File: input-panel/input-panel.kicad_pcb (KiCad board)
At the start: 2 copper layers, 81.3 x 54.6 mm, 11 parts, among them J1 Conn_01x07_Male

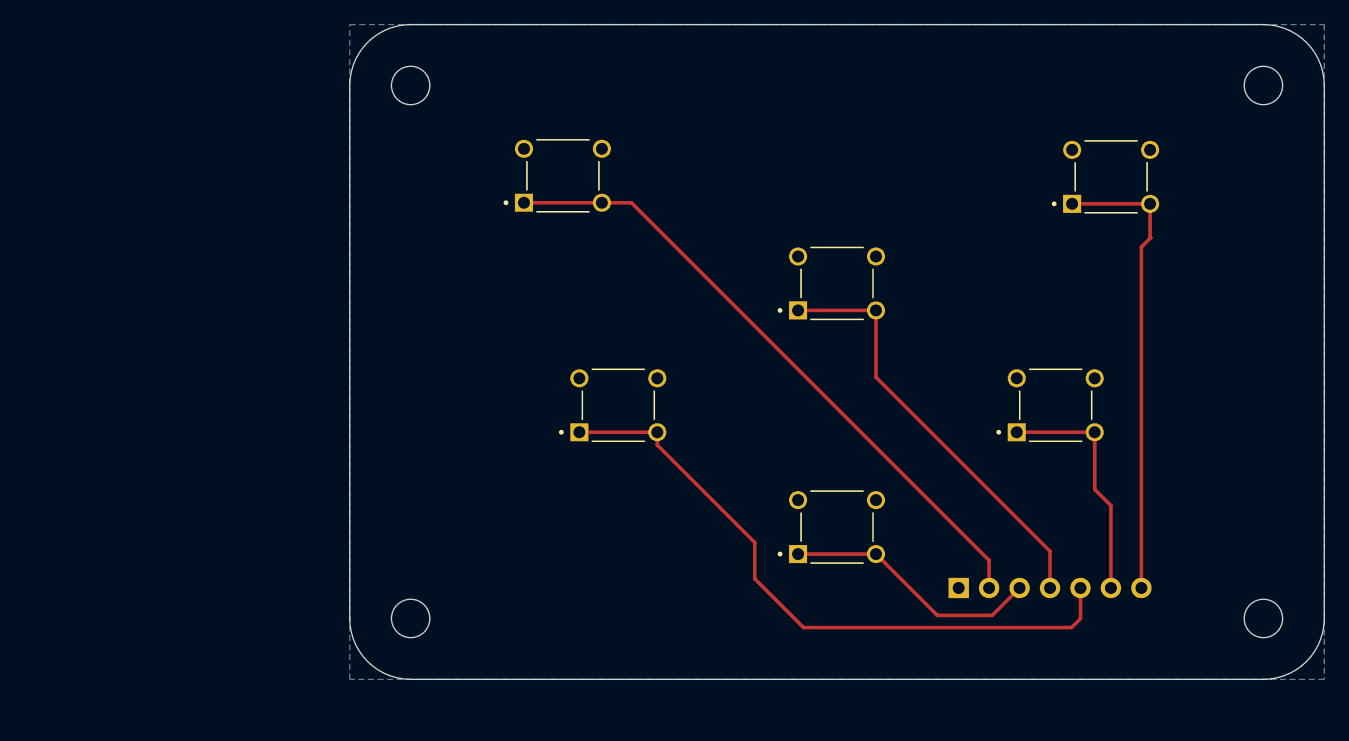
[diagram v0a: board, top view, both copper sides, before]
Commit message: re-designed input panel PCB
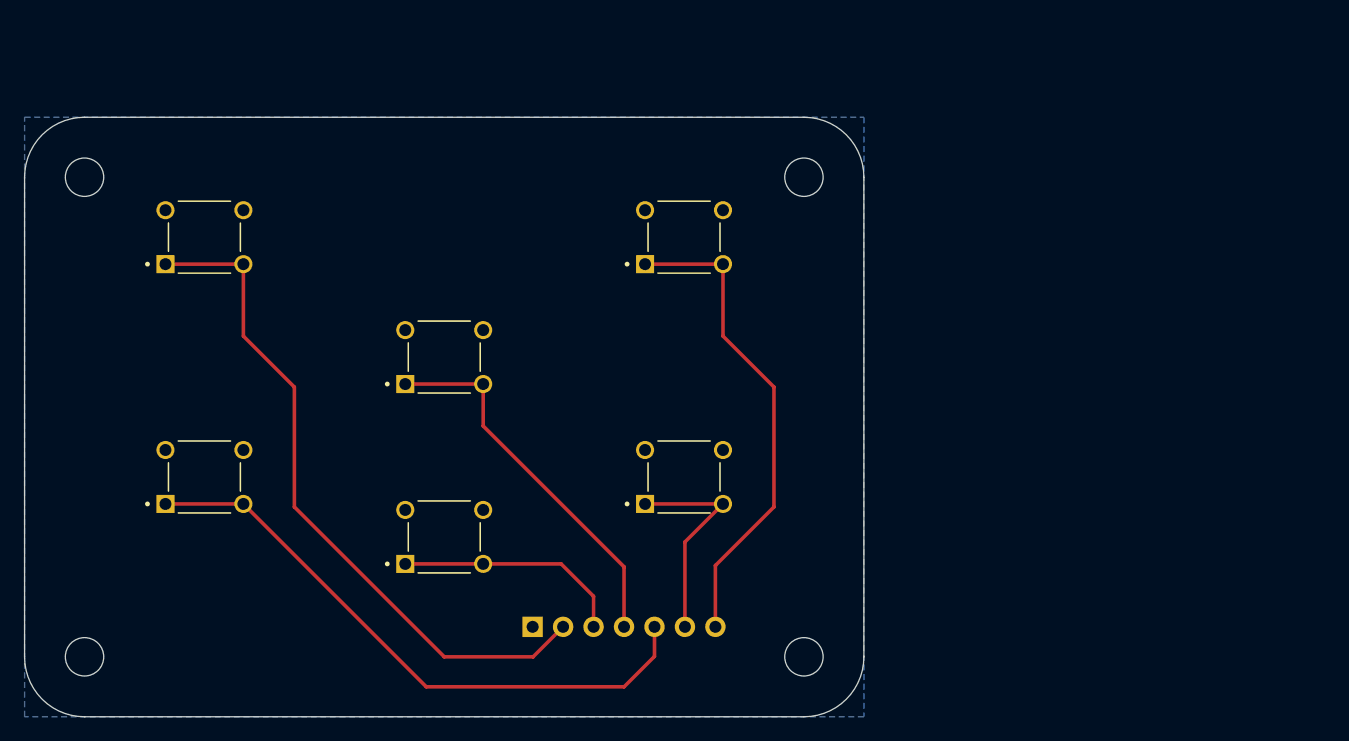
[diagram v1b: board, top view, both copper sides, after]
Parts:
- moved H4 39.1 mm to (172.5, 77.5)
- moved H2 38.5 mm to (172.5, 117.5)
- moved S6 36.0 mm to (162.5, 82.5)
- moved J1 35.7 mm to (149.9, 115.0)
- moved S4 35.0 mm to (122.5, 102.5)
- moved S3 33.3 mm to (142.5, 92.5)
- moved S2 32.8 mm to (142.5, 107.5)
- moved S5 31.6 mm to (162.5, 102.5)
- moved S1 30.3 mm to (122.5, 82.5)
- moved H1 28.3 mm to (112.5, 77.5)
- moved H3 27.4 mm to (112.5, 117.5)
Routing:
- net Net-(J1-Pad4): track 35.7 -> 31.6 mm
- net Net-(J1-Pad2): track 53.5 -> 57.1 mm
- net Net-(J1-Pad5): track 53.8 -> 50.6 mm
- net Net-(J1-Pad3): track 21.5 -> 19.4 mm
- net Net-(J1-Pad6): track 20.1 -> 18.1 mm
- net Net-(J1-Pad7): track 38.9 -> 40.5 mm
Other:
- board size 81.3 x 54.6 mm -> 70 x 50 mm
- board text added: "Input Panel"
- board text added: "pyroDirector v0.1"
